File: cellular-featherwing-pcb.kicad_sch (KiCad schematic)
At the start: 1 part, among them U1 BG96

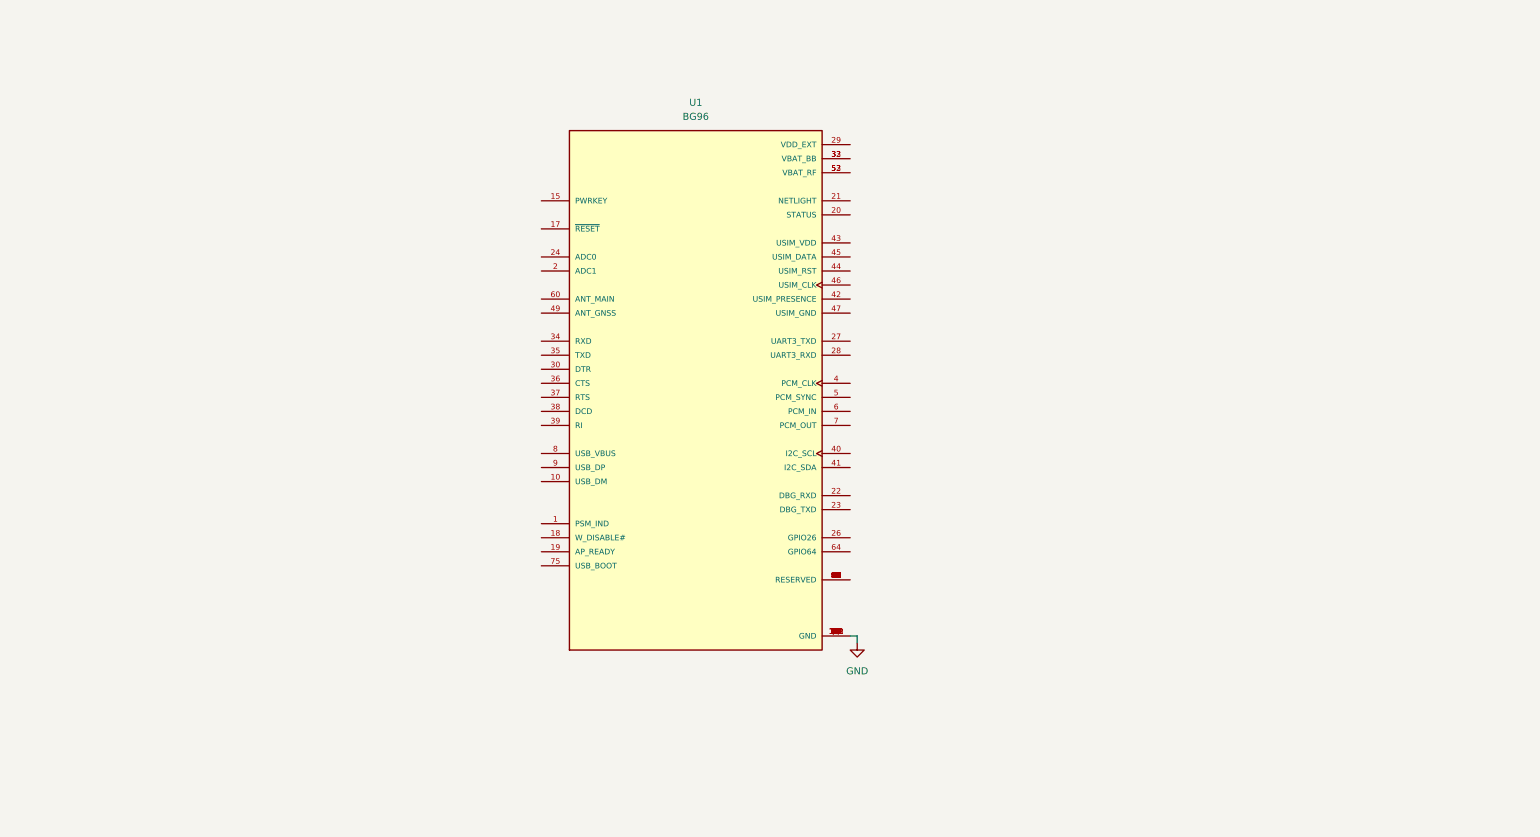
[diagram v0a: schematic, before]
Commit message: Footprints for all major components
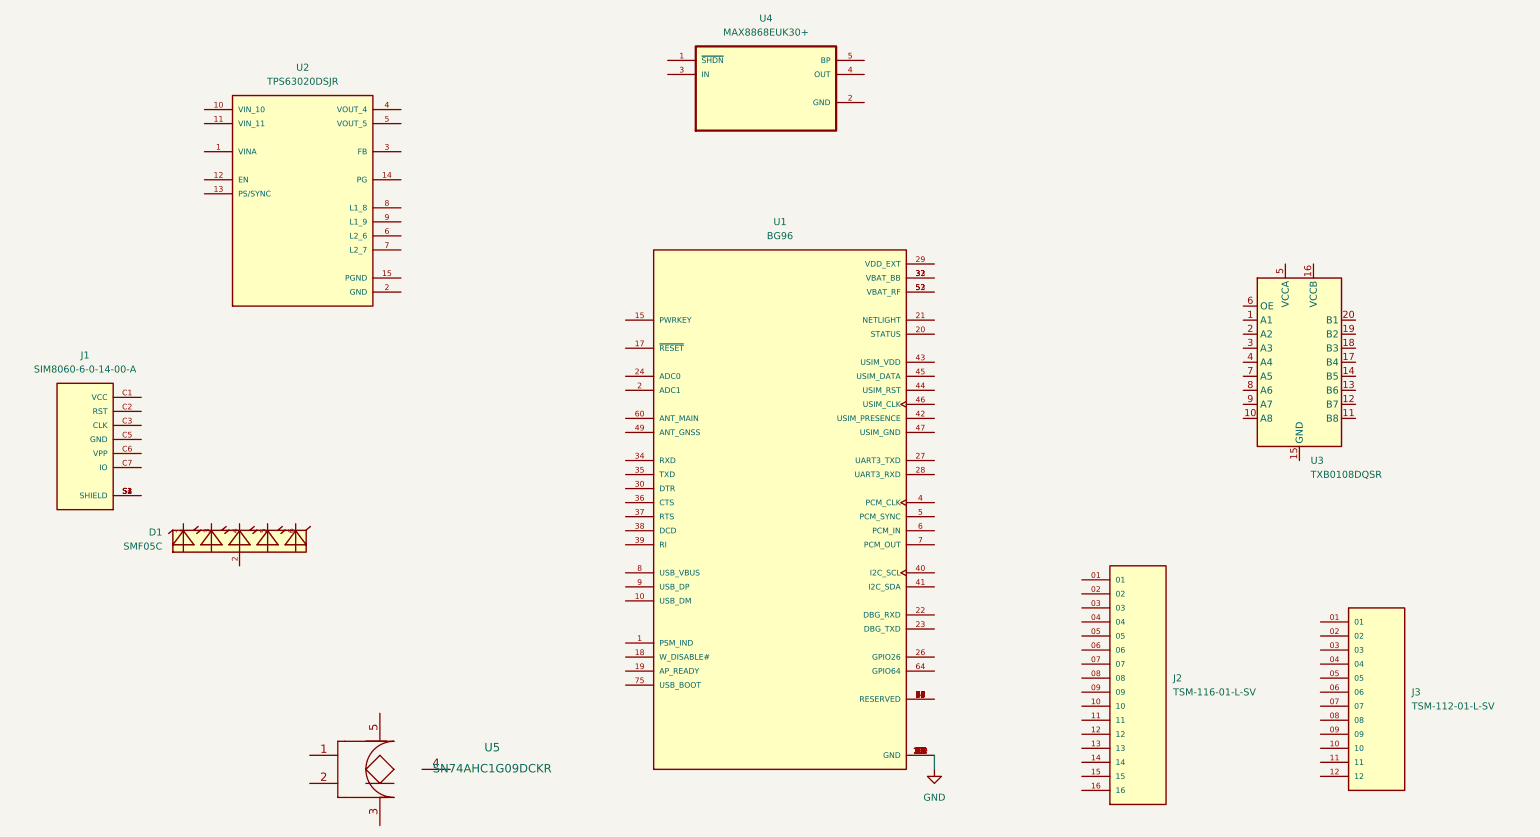
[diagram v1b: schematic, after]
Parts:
- added D1: SMF05C, SC70-6, symbol SMF05C:SMF05C
- added J1: SIM8060-6-0-14-00-A, GCT_SIM8060-6-0-14-00-A, symbol SIM8060-6-0-14-00-A:SIM8060-6-0-14-00-A
- added J2: TSM-116-01-L-SV, SAMTEC_TSM-116-01-L-SV, symbol TSM-116-01-L-SV:TSM-116-01-L-SV
- added J3: TSM-112-01-L-SV, SAMTEC_TSM-112-01-L-SV, symbol TSM-112-01-L-SV:TSM-112-01-L-SV
- added U2: TPS63020DSJR, IC_TPS63020DSJR, symbol TPS63020DSJR:TPS63020DSJR
- added U3: TXB0108DQSR, Package_SON:USON-20_2x4mm_P0.4mm, symbol Logic_LevelTranslator:TXB0108DQSR
- added U4: MAX8868EUK30+, SOT95P280X145-5N, symbol MAX8868EUK30_:MAX8868EUK30+
- added U5: SN74AHC1G09DCKR, SN74AHC1G09DCKR:SN74AHC1G09DCKR, symbol 2023-01-14_23-42-37:SN74AHC1G09DCKR
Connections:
- new net: J1.S1 (SHIELD), J1.S2 (SHIELD), J1.S3 (SHIELD), J1.S4 (SHIELD)
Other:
- moved on the sheet: U1

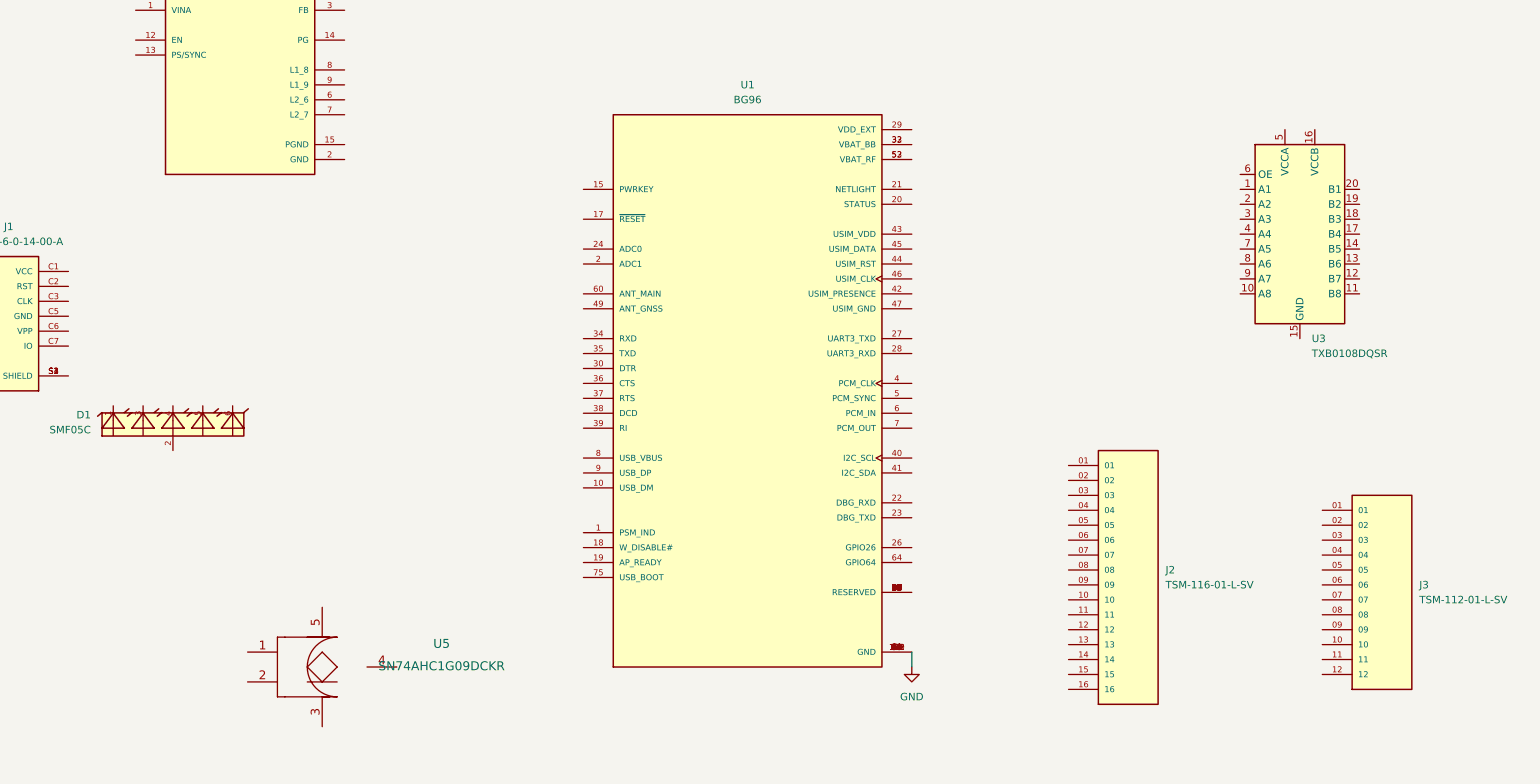
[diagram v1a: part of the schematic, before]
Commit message: Add pn for gate
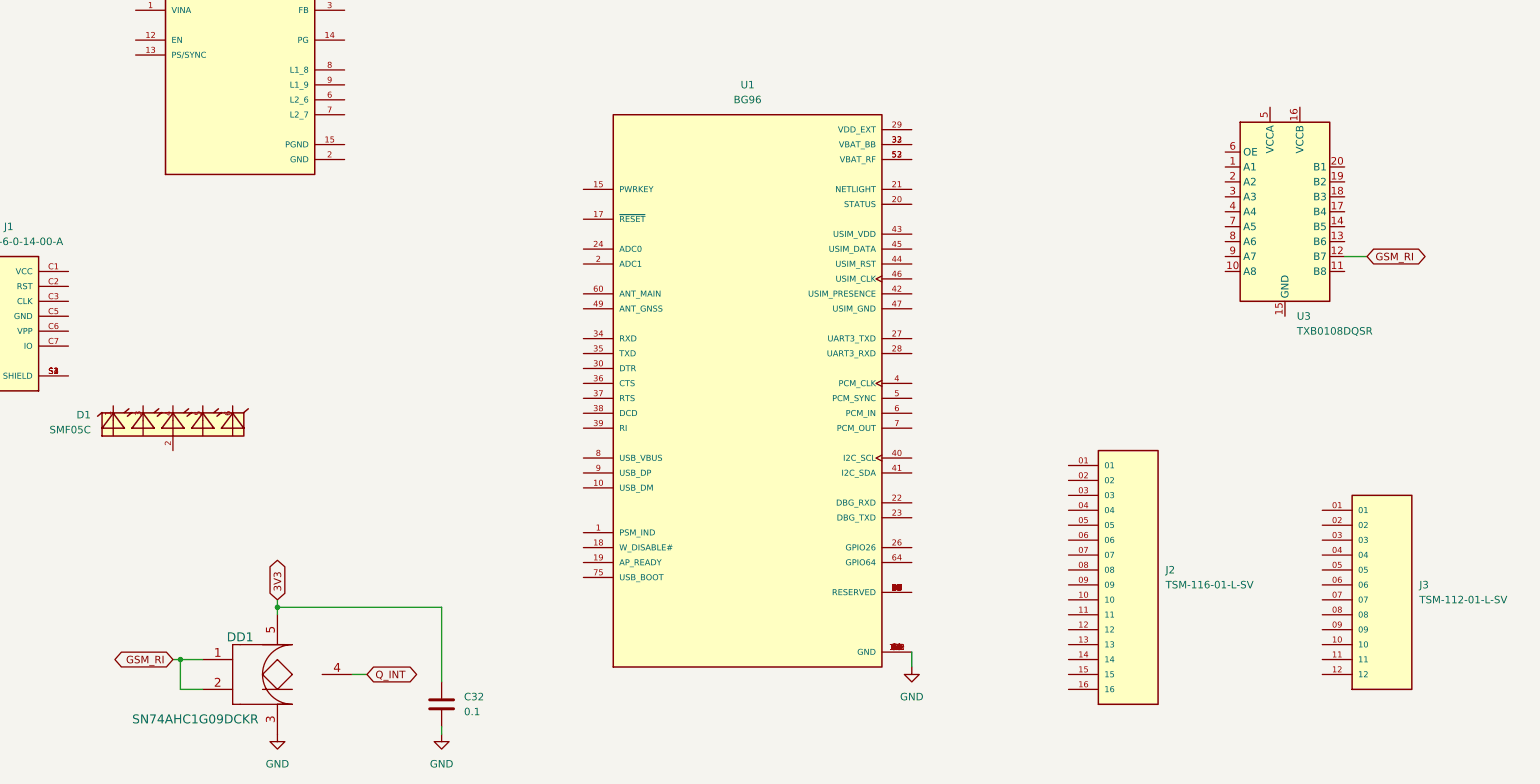
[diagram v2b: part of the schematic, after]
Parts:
- added C32: 0.1, symbol Device:C
- DD1: renamed from U5; MPN (none) -> SN74AHC1G09DCKR
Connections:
- net GND: now also DD1.3 (GND), C32.2
- net GSM_RI: now reaches DD1.1 (A)
- net GSM_RI: now also DD1.2 (B), U3.12 (B7)
- net Q_INT: now reaches DD1.4 (Y)
- net 3V3: now reaches DD1.5 (VCC)
- net 3V3: now also C32.1
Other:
- moved on the sheet: DD1, U3
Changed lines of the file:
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@@
 (kicad_sch (version 20211123) (generator eeschema)
   (paper "A4")
+  (junction (at 55.88 152.4) (diameter 0) (color 0 0 0 0)
+  )
+  (junction (at 72.39 143.51) (diameter 0) (color 0 0 0 0)
+  )
+  (wire (pts (xy 55.88 152.4) (xy 55.88 157.48))
+    (stroke (width 0) (type default) (color 0 0 0 0))
+  )
   (wire (pts (xy 180.34 151.13) (xy 180.34 153.67))
     (stroke (width 0) (type default) (color 0 0 0 0))
+  )
+  (wire (pts (xy 72.39 142.24) (xy 72.39 143.51))
+    (stroke (width 0) (type default) (color 0 0 0 0))
+  )
+  (wire (pts (xy 100.33 143.51) (xy 100.33 156.21))
+    (stroke (width 0) (type default) (color 0 0 0 0))
+  )
+  (wire (pts (xy 54.61 152.4) (xy 55.88 152.4))
+    (stroke (width 0) (type default) (color 0 0 0 0))
+  )
+  (wire (pts (xy 55.88 157.48) (xy 59.69 157.48))
+    (stroke (width 0) (type default) (color 0 0 0 0))
+  )
+  (wire (pts (xy 85.09 154.94) (xy 87.63 154.94))
+    (stroke (width 0) (type default) (color 0 0 0 0))
+  )
+  (wire (pts (xy 72.39 143.51) (xy 72.39 144.78))
+    (stroke (width 0) (type default) (color 0 0 0 0))
+  )
+  (wire (pts (xy 100.33 163.83) (xy 100.33 165.1))
+    (stroke (width 0) (type default) (color 0 0 0 0))
+  )
+  (wire (pts (xy 254 83.82) (xy 257.81 83.82))
+    (stroke (width 0) (type default) (color 0 0 0 0))
+  )
+  (wire (pts (xy 55.88 152.4) (xy 59.69 152.4))
+    (stroke (width 0) (type default) (color 0 0 0 0))
+  )
+  (wire (pts (xy 72.39 143.51) (xy 100.33 143.51))
+    (stroke (width 0) (type default) (color 0 0 0 0))
+  )
+  (global_label "Q_INT" (shape bidirectional) (at 87.63 154.94 0) (fields_autoplaced)
+    (effects (font (size 1.27 1.27)) (justify left))
+    (property "Intersheet References" "${INTERSHEET_REFS}" (id 0) (at 95.2441 154.8606 0)
+      (effects (font (size 1.27 1.27)) (justify left) hide)
+    )
+  )
+  (global_label "GSM_RI" (shape bidirectional) (at 54.61 152.4 180) (fields_autoplaced)
+    (effects (font (size 1.27 1.27)) (justify right))
+    (property "Intersheet References" "${INTERSHEET_REFS}" (id 0) (at 45.4236 152.3206 0)
+      (effects (font (size 1.27 1.27)) (justify right) hide)
+    )
+  )
+  (global_label "3V3" (shape bidirectional) (at 72.39 142.24 90) (fields_autoplaced)
+    (effects (font (size 1.27 1.27)) (justify left))
+    (property "Intersheet References" "${INTERSHEET_REFS}" (id 0) (at 72.3106 136.3193 90)
+      (effects (font (size 1.27 1.27)) (justify left) hide)
+    )
+  )
+  (global_label "GSM_RI" (shape bidirectional) (at 257.81 83.82 0) (fields_autoplaced)
+    (effects (font (size 1.27 1.27)) (justify left))
+    (property "Intersheet References" "${INTERSHEET_REFS}" (id 0) (at 266.9964 83.7406 0)
+      (effects (font (size 1.27 1.27)) (justify left) hide)
+    )
   )
   (symbol (lib_id "TSM-112-01-L-SV:TSM-112-01-L-SV") (at 260.35 139.7 0) (unit 1)
@@
     (pin "4")
     (pin "5")
+  )
+  (symbol (lib_id "Device:C") (at 100.33 160.02 0) (unit 1)
+    (in_bom yes) (on_board yes) (fields_autoplaced)
+    (property "Reference" "C32" (id 0) (at 104.14 158.7499 0)
+      (effects (font (size 1.27 1.27)) (justify left))
+    )
+    (property "Value" "0.1" (id 1) (at 104.14 161.2899 0)
+      (effects (font (size 1.27 1.27)) (justify left))
+    )
+    (property "Footprint" "" (id 2) (at 101.2952 163.83 0)
+      (effects (font (size 1.27 1.27)) hide)
+    )
+    (property "Datasheet" "~" (id 3) (at 100.33 160.02 0)
+      (effects (font (size 1.27 1.27)) hide)
+    )
+    (pin "1")
+    (pin "2")
   )
   (symbol (lib_id "TSM-116-01-L-SV:TSM-116-01-L-SV") (at 217.17 137.16 0) (unit 1)
@@
     (pin "5")
     (pin "6")
+  )
+  (symbol (lib_id "power:GND") (at 72.39 165.1 0) (unit 1)
+    (in_bom yes) (on_board yes) (fields_autoplaced)
+    (property "Reference" "#PWR?" (id 0) (at 72.39 171.45 0)
+      (effects (font (size 1.27 1.27)) hide)
+    )
+    (property "Value" "GND" (id 1) (at 72.39 170.18 0))
+    (property "Footprint" "" (id 2) (at 72.39 165.1 0)
+      (effects (font (size 1.27 1.27)) hide)
+    )
+    (property "Datasheet" "" (id 3) (at 72.39 165.1 0)
+      (effects (font (size 1.27 1.27)) hide)
+    )
+    (pin "1")
   )
   (symbol (lib_id "BG96:BG96") (at 152.4 105.41 0) (unit 1)
@@
     (pin "99")
   )
-  (symbol (lib_id "2023-01-14_23-42-37:SN74AHC1G09DCKR") (at 80.01 153.67 0) (unit 1)
-    (in_bom yes) (on_board yes) (fields_autoplaced)
-    (property "Reference" "U5" (id 0) (at 100.33 149.7052 0)
+  (symbol (lib_id "power:GND") (at 100.33 165.1 0) (unit 1)
+    (in_bom yes) (on_board yes) (fields_autoplaced)
+    (property "Reference" "#PWR?" (id 0) (at 100.33 171.45 0)
+      (effects (font (size 1.27 1.27)) hide)
+    )
+    (property "Value" "GND" (id 1) (at 100.33 170.18 0))
+    (property "Footprint" "" (id 2) (at 100.33 165.1 0)
+      (effects (font (size 1.27 1.27)) hide)
+    )
+    (property "Datasheet" "" (id 3) (at 100.33 165.1 0)
+      (effects (font (size 1.27 1.27)) hide)
+    )
+    (pin "1")
+  )
+  (symbol (lib_id "2023-01-14_23-42-37:SN74AHC1G09DCKR") (at 72.39 154.94 0) (unit 1)
+    (in_bom yes) (on_board yes)
+    (property "Reference" "DD1" (id 0) (at 66.04 148.59 0)
       (effects (font (size 1.524 1.524)))
     )
-    (property "Value" "SN74AHC1G09DCKR" (id 1) (at 100.33 153.5152 0)
+    (property "Value" "SN74AHC1G09DCKR" (id 1) (at 58.42 162.56 0)
       (effects (font (size 1.524 1.524)))
     )
-    (property "Footprint" "SN74AHC1G09DCKR:SN74AHC1G09DCKR" (id 2) (at 80.01 155.194 0)
+    (property "Footprint" "SN74AHC1G09DCKR:SN74AHC1G09DCKR" (id 2) (at 72.39 156.464 0)
       (effects (font (size 1.524 1.524)) hide)
     )
-    (property "Datasheet" "" (id 3) (at 80.01 153.67 0)
-      (effects (font (size 1.524 1.524)))
+    (property "Datasheet" "" (id 3) (at 72.39 154.94 0)
+      (effects (font (size 0 0)))
+    )
+    (property "MPN" "SN74AHC1G09DCKR" (id 4) (at 72.39 154.94 0)
+      (effects (font (size 1.27 1.27)) hide)
     )
     (pin "1")
@@
     (pin "9")
   )
-  (symbol (lib_id "Logic_LevelTranslator:TXB0108DQSR") (at 246.38 80.01 0) (unit 1)
-    (in_bom yes) (on_board yes) (fields_autoplaced)
-    (property "Reference" "U3" (id 0) (at 248.3994 97.79 0)
-      (effects (font (size 1.27 1.27)) (justify left))
-    )
-    (property "Value" "TXB0108DQSR" (id 1) (at 248.3994 100.33 0)
-      (effects (font (size 1.27 1.27)) (justify left))
-    )
-    (property "Footprint" "Package_SON:USON-20_2x4mm_P0.4mm" (id 2) (at 246.38 99.06 0)
-      (effects (font (size 1.27 1.27)) hide)
-    )
-    (property "Datasheet" "http://www.ti.com/lit/ds/symlink/txb0108.pdf" (id 3) (at 246.38 82.55 0)
+  (symbol (lib_id "Logic_LevelTranslator:TXB0108DQSR") (at 243.84 76.2 0) (unit 1)
+    (in_bom yes) (on_board yes) (fields_autoplaced)
+    (property "Reference" "U3" (id 0) (at 245.8594 93.98 0)
+      (effects (font (size 1.27 1.27)) (justify left))
+    )
+    (property "Value" "TXB0108DQSR" (id 1) (at 245.8594 96.52 0)
+      (effects (font (size 1.27 1.27)) (justify left))
+    )
+    (property "Footprint" "Package_SON:USON-20_2x4mm_P0.4mm" (id 2) (at 243.84 95.25 0)
+      (effects (font (size 1.27 1.27)) hide)
+    )
+    (property "Datasheet" "http://www.ti.com/lit/ds/symlink/txb0108.pdf" (id 3) (at 243.84 78.74 0)
       (effects (font (size 1.27 1.27)) hide)
     )
@@
       (reference "#PWR0101") (unit 1) (value "GND") (footprint "")
     )
+    (path "/73d072bf-f827-4b2a-89e2-039207f93fd3"
+      (reference "#PWR?") (unit 1) (value "GND") (footprint "")
+    )
+    (path "/cd1a3e20-6688-488d-b930-eb8fc8b01e25"
+      (reference "#PWR?") (unit 1) (value "GND") (footprint "")
+    )
+    (path "/5b635a22-c0b1-4db5-9d17-07af64d1041e"
+      (reference "C32") (unit 1) (value "0.1") (footprint "")
+    )
     (path "/733651b1-169f-4ad3-9294-b74c4483ba41"
       (reference "D1") (unit 1) (value "SMF05C") (footprint "SC70-6")
     )
+    (path "/dad88395-9b9e-4e40-937c-763bc7b579d0"
+      (reference "DD1") (unit 1) (value "SN74AHC1G09DCKR") (footprint "SN74AHC1G09DCKR:SN74AHC1G09DCKR")
+    )
     (path "/601f9e17-50e9-447a-9492-85ac68392029"
       (reference "J1") (unit 1) (value "SIM8060-6-0-14-00-A") (footprint "GCT_SIM8060-6-0-14-00-A")
@@
       (reference "U4") (unit 1) (value "MAX8868EUK30+") (footprint "SOT95P280X145-5N")
     )
-    (path "/dad88395-9b9e-4e40-937c-763bc7b579d0"
-      (reference "U5") (unit 1) (value "SN74AHC1G09DCKR") (footprint "SN74AHC1G09DCKR:SN74AHC1G09DCKR")
-    )
-  )
+  )

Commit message: Add ufl connector
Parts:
- added J4, J5: U.FL-R-SMT(10), HRS_U.FL-R-SMT(10), symbol U.FL-R-SMT_10_:U.FL-R-SMT(10)
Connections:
- new net: J5.2, J5.3
- new net: J4.2, J4.3
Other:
- moved on the sheet: C32, D1, DD1, J1, J2, J3, U1, U2, U3, U4

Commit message: Wired up bg96 in schematic
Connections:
- net GND: now also J2.04, U1.42 (USIM_PRESENCE), U1.47 (USIM_GND)
- net VBAT: now reaches J3.01
- net 5V: now reaches J3.03
- net ENABLE: now reaches J3.04
- net GSM_RI_EXT: now reaches J3.05
- net GSM_TXD_ESP_RTS: now reaches J3.06
- net GSM_RXD_ESP_CTS: now reaches J3.07
- net MODEM_ON: now reaches J3.09
- net GSM_DTR_EXT: now reaches J3.10
- net I2C_SCL: now reaches J3.11
- net I2C_SDA: now reaches J3.12
- net VDD: now reaches J2.02
- net GMS_STATUS_EXT: now reaches J2.05
- net Q_INT_EXT: now reaches J2.09
- net GSM_DCD_EXT: now reaches J2.10
- net GSM_TXD_ESP32: now reaches J2.14
- net GSM_RXD_ESP32: now reaches J2.15
- net USB_DN_GSM: now reaches U1.10 (USB_DM)
- net ON_PIN: now reaches U1.15 (PWRKEY)
- net GSM_STATUS_INT: now reaches U1.20 (STATUS)
- net GSM_NET: now reaches U1.21 (NETLIGHT)
- net DBG_RXD: now reaches U1.22 (DBG_RXD)
- net DBG_TXD: now reaches U1.23 (DBG_TXD)
- net GPS_TXD: now reaches U1.27 (UART3_TXD)
- net GPS_RXD: now reaches U1.28 (UART3_RXD)
- net VDD_EXT: now reaches U1.29 (VDD_EXT)
- net DTR: now reaches U1.30 (DTR)
- net VBAT_BB: now reaches U1.32 (VBAT_BB), U1.33 (VBAT_BB)
- net RXD: now reaches U1.34 (RXD)
- net TXD: now reaches U1.35 (TXD)
- net CTS: now reaches U1.36 (CTS)
- net RTS: now reaches U1.37 (RTS)
- net DCD: now reaches U1.38 (DCD)
- net RI: now reaches U1.39 (RI)
- net SIM_VDD: now reaches U1.43 (USIM_VDD)
- net SIM_RST: now reaches U1.44 (USIM_RST)
- net SIM_DATA: now reaches U1.45 (USIM_DATA)
- net SIM_CLK: now reaches U1.46 (USIM_CLK)
- net GPS_ANT: now reaches U1.49 (ANT_GNSS)
- net VBAT_RF: now reaches U1.52 (VBAT_RF), U1.53 (VBAT_RF)
- net GSM_ANT: now reaches U1.60 (ANT_MAIN)
- net USB_BOOT: now reaches U1.75 (USB_BOOT)
- net USB_VBUS_GSM: now reaches U1.8 (USB_VBUS)
- net USB_DP_GSM: now reaches U1.9 (USB_DP)
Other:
- moved on the sheet: J2, J3

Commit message: schematic updates
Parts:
- added C28, C29: 0.1, symbol Device:C
- U3: MPN (none) -> TXB0108DQSR
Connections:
- net 3V3: now also U3.16 (VCCB), C28.1
- net DCD: now also U3.8 (A6)
- net DTR: now also U3.7 (A5)
- net GND: now also U3.15 (GND), C28.2, C29.2
- net GSM_STATUS_INT: now also U3.10 (A8)
- net RI: now also U3.9 (A7)
- net RXD: now also U3.1 (A1)
- net TXD: now also U3.2 (A2)
- net VDD_EXT: now also U3.5 (VCCA), U3.6 (OE), C29.1
- net GSM_STATUS: now reaches U3.11 (B8)
- net GSM_DCD: now reaches U3.13 (B6)
- net GSM_DTR: now reaches U3.14 (B5)
- net GSM_CTS: now reaches U3.17 (B4)
- net GSM_RTS: now reaches U3.18 (B3)
- net GSM_TXD: now reaches U3.19 (B2)
- net GSM_RXD: now reaches U3.20 (B1)
- net RTS_GPS_RXD: now reaches U3.3 (A3)
- net CTS_GPS_TXD: now reaches U3.4 (A4)
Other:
- moved on the sheet: U3

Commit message: More progress
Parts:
- added VT3, VT4: DTC043TEBTL, ul_DTC043TEBTL:DTC043TEBTL, symbol dtc043tebtl:DTC043TEBTL
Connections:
- net GND: now also VT3.3, VT4.3
- net ON_PIN: now also VT4.1, VT4.2
- new net: VT3.1, VT3.2
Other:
- moved on the sheet: C28, C29, J2, J3, U3
